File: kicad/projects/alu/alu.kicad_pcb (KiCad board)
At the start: 2 copper layers, 203.2 x 97.8 mm, 56 parts, among them J1 ACC_CONTENTS, J2 RES_AEQB_CRYBRW_OUT, J3 Control_signal_backplane, J4 Bus_connection, J5 Aux_connection, J6 TOP_POWER, J7 LED_CONTROL, U1 74HC04, U10 74HC157, U11 74HC157, U12 74HC245, U13 74HC245, U2 74LS181, U3 74LS181, U4 74HCT245, U5 74LS181, U6 74HCT245, U7 74LS181, U8 74HC157, U9 74HC157

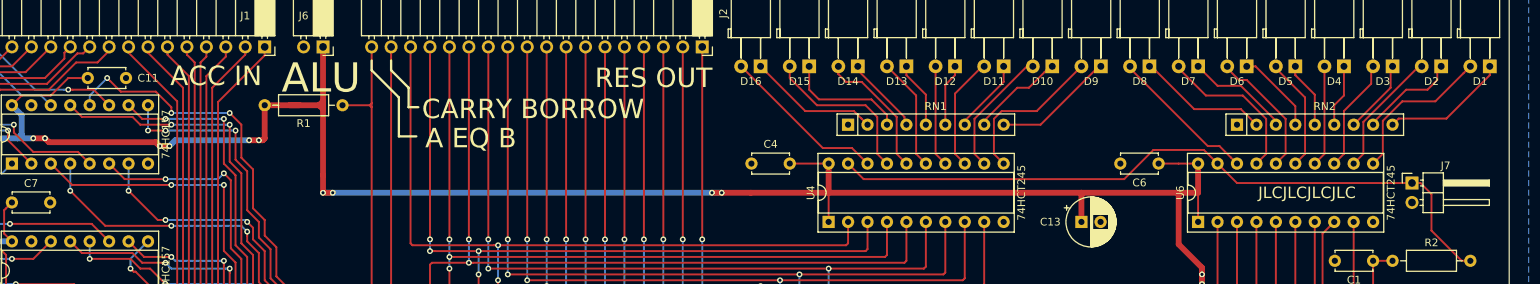
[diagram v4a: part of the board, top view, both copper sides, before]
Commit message: Better labels on ALU. Top power and LED control on register.
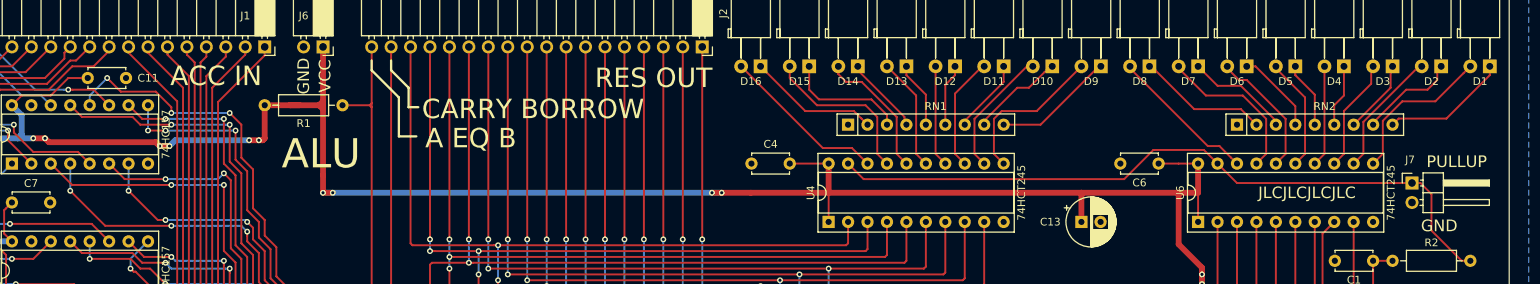
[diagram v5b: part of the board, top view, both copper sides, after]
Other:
- board text added: "GND"
- board text added: "PULLUP"
- board text added: "VCC"
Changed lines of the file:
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@@
   (general
     (thickness 1.6)
-    (drawings 22)
+    (drawings 26)
     (tracks 2059)
     (zones 0)
@@
     (descr "Through hole angled pin header, 1x02, 2.54mm pitch, 6mm pin length, single row")
     (tags "Through hole angled pin header THT 1x02 2.54mm single row")
-    (fp_text reference J7 (at 4.385 -2.27) (layer F.SilkS)
+    (fp_text reference J7 (at -0.254 -3.048) (layer F.SilkS)
       (effects (font (size 1 1) (thickness 0.15)))
     )
@@
     )
   )
+  (gr_text GND (at 247.396 81.788) (layer F.SilkS)
+    (effects (font (size 1.524 1.524) (thickness 0.254)))
+  )
+  (gr_text PULLUP (at 249.682 73.406) (layer F.SilkS)
+    (effects (font (size 1.524 1.524) (thickness 0.254)))
+  )
+  (gr_text GND (at 99.06 62.23 90) (layer F.SilkS)
+    (effects (font (size 1.524 1.524) (thickness 0.254)))
+  )
+  (gr_text VCC (at 101.854 62.23 90) (layer F.SilkS)
+    (effects (font (size 1.524 1.524) (thickness 0.254)))
+  )
   (gr_arc (start 55.245 144.145) (end 53.34 144.145) (angle -90) (layer Edge.Cuts) (width 0.05))
   (gr_arc (start 55.245 50.165) (end 55.245 48.26) (angle -90) (layer Edge.Cuts) (width 0.05))
@@
     (effects (font (size 1.5 1.5) (thickness 0.3)))
   )
-  (gr_text ALU (at 101.346 62.484) (layer F.SilkS)
+  (gr_text ALU (at 101.346 72.39) (layer F.SilkS)
     (effects (font (size 3.81 3.81) (thickness 0.381)))
   )
@@
   (segment (start 69.088 89.408) (end 61.468 89.408) (width 0.254) (layer F.Cu) (net 87))
   (via (at 59.182 89.408012) (size 0.762) (drill 0.4) (layers F.Cu B.Cu) (net 87))
+  (segment (start 59.182012 89.408) (end 59.182 89.408012) (width 0.254) (layer B.Cu) (net 87))
+  (segment (start 61.468 89.408) (end 59.182012 89.408) (width 0.254) (layer B.Cu) (net 87))
+  (segment (start 59.182 88.842327) (end 59.182 89.408012) (width 0.254) (layer F.Cu) (net 87))
+  (segment (start 58.42 64.008) (end 58.42 84.711981) (width 0.254) (layer F.Cu) (net 87))
+  (segment (start 59.182 85.473981) (end 59.182 88.842327) (width 0.254) (layer F.Cu) (net 87))
+  (segment (start 71.12 58.42) (end 69.342 60.198) (width 0.254) (layer F.Cu) (net 87))
+  (segment (start 69.342 60.198) (end 68.58 60.198) (width 0.254) (layer F.Cu) (net 87))
+  (segment (start 68.58 60.198) (end 65.532 63.246) (width 0.254) (layer F.Cu) (net 87))
   (segment (start 65.532 63.246) (end 59.182 63.246) (width 0.254) (layer F.Cu) (net 87))
   (segment (start 58.42 84.711981) (end 59.182 85.473981) (width 0.254) (layer F.Cu) (net 87))
-  (segment (start 59.182 85.473981) (end 59.182 88.842327) (width 0.254) (layer F.Cu) (net 87))
-  (segment (start 58.42 64.008) (end 58.42 84.711981) (width 0.254) (layer F.Cu) (net 87))
   (segment (start 59.182 63.246) (end 58.42 64.008) (width 0.254) (layer F.Cu) (net 87))
-  (segment (start 69.508001 59.269999) (end 65.532 63.246) (width 0.254) (layer F.Cu) (net 87))
-  (segment (start 59.182 88.842327) (end 59.182 89.408012) (width 0.254) (layer F.Cu) (net 87))
-  (segment (start 70.270001 59.269999) (end 69.508001 59.269999) (width 0.254) (layer F.Cu) (net 87))
-  (segment (start 71.12 58.42) (end 70.270001 59.269999) (width 0.254) (layer F.Cu) (net 87))
-  (segment (start 59.182012 89.408) (end 59.182 89.408012) (width 0.254) (layer B.Cu) (net 87))
-  (segment (start 61.468 89.408) (end 59.182012 89.408) (width 0.254) (layer B.Cu) (net 87))
   (segment (start 62.23 90.17) (end 63.5 91.44) (width 0.254) (layer F.Cu) (net 88))
-  (segment (start 69.342 60.452) (end 65.786 64.008) (width 0.254) (layer F.Cu) (net 88))
-  (segment (start 73.66 58.928) (end 72.136 60.452) (width 0.254) (layer F.Cu) (net 88))
-  (segment (start 72.136 60.452) (end 69.342 60.452) (width 0.254) (layer F.Cu) (net 88))
+  (segment (start 68.834 60.96) (end 65.786 64.008) (width 0.254) (layer F.Cu) (net 88))
   (segment (start 59.182 84.582) (end 60.198 85.598) (width 0.254) (layer F.Cu) (net 88))
+  (segment (start 71.628 60.96) (end 68.834 60.96) (width 0.254) (layer F.Cu) (net 88))
+  (segment (start 60.198 89.662) (end 60.706 90.17) (width 0.254) (layer F.Cu) (net 88))
   (segment (start 73.66 58.42) (end 73.66 58.928) (width 0.254) (layer F.Cu) (net 88))
-  (segment (start 65.786 64.008) (end 59.436 64.008) (width 0.254) (layer F.Cu) (net 88))
+  (segment (start 73.66 58.928) (end 71.628 60.96) (width 0.254) (layer F.Cu) (net 88))
   (segment (start 59.182 64.262) (end 59.182 84.582) (width 0.254) (layer F.Cu) (net 88))
+  (segment (start 65.786 64.008) (end 59.436 64.008) (width 0.254) (layer F.Cu) (net 88))
   (segment (start 59.436 64.008) (end 59.182 64.262) (width 0.254) (layer F.Cu) (net 88))
-  (segment (start 60.706 90.17) (end 62.23 90.17) (width 0.254) (layer F.Cu) (net 88))
   (segment (start 60.198 85.598) (end 60.198 89.662) (width 0.254) (layer F.Cu) (net 88))
-  (segment (start 60.198 89.662) (end 60.706 90.17) (width 0.254) (layer F.Cu) (net 88))
+  (segment (start 60.706 90.17) (end 62.23 90.17) (width 0.254) (layer F.Cu) (net 88))
   (segment (start 68.834 98.806) (end 66.04 101.6) (width 0.254) (layer F.Cu) (net 89))
   (segment (start 75.438 98.806) (end 68.834 98.806) (width 0.254) (layer F.Cu) (net 89))

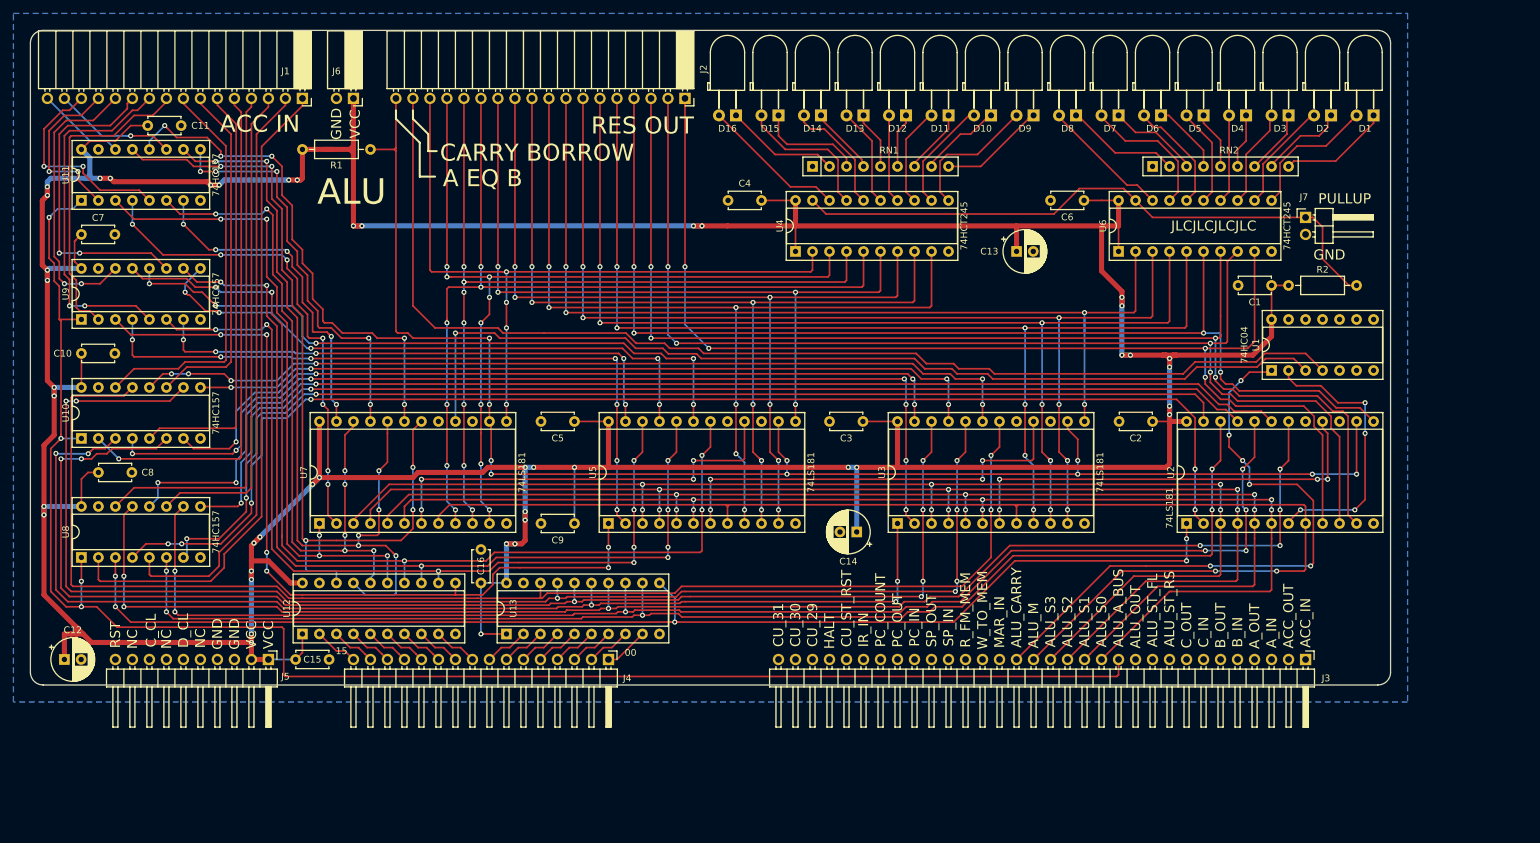
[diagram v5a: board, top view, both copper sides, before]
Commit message: Add HCT output buffer from 74LS181 on ALU.
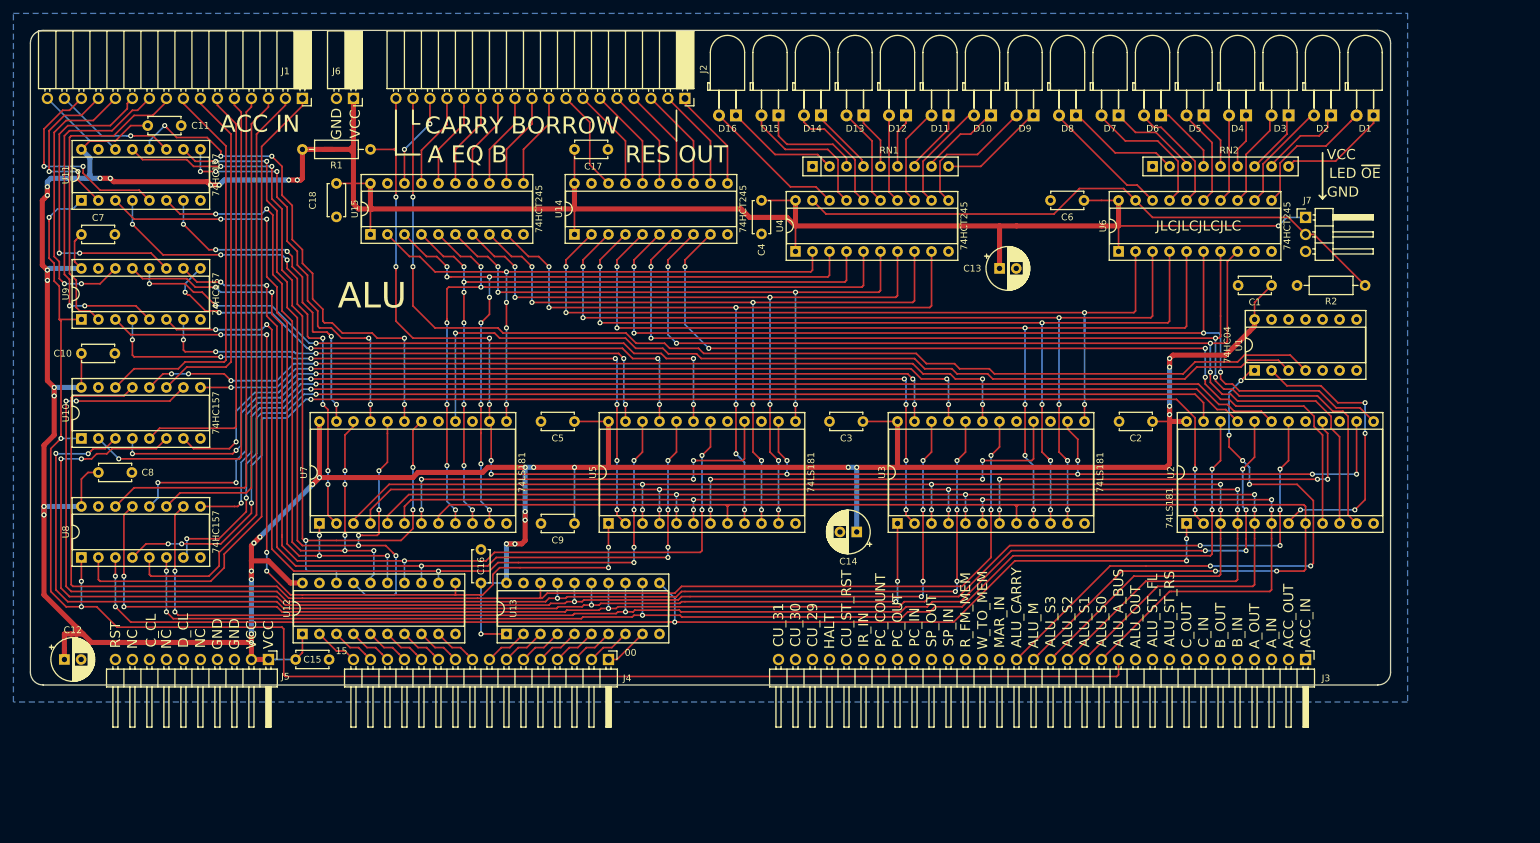
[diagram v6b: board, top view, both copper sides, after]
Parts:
- added C17: 0.1uF, Capacitor_THT:C_Disc_D4.7mm_W2.5mm_P5.00mm, F.Cu at (134.6, 66.0)
- added C18: 0.1uF, Capacitor_THT:C_Disc_D4.7mm_W2.5mm_P5.00mm, F.Cu at (99.1, 71.1)
- added U14: 74HCT245, Package_DIP:DIP-20_W7.62mm_Socket, F.Cu at (134.6, 78.7)
- added U15: 74HCT245, Package_DIP:DIP-20_W7.62mm_Socket, F.Cu at (104.1, 78.7)
- J7: footprint Connector_PinHeader_2.54mm:PinHeader_1x02_P2.54mm_Horizontal -> Connector_PinHeader_2.54mm:PinHeader_1x03_P2.54mm_Horizontal
- moved R2 11.4 mm to (252.7, 86.4), turned to 180 degrees
- moved C13 3.59 mm to (198.1, 83.8)
- moved U1 2.54 mm to (236.2, 99.1)
- turned C4 to 270 degrees
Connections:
- J2 pad 1: /RES_00 -> /RES_HC_BUF_00
- J2 pad 10: /RES_09 -> /RES_HC_BUF_09
- J2 pad 11: /RES_10 -> /RES_HC_BUF_10
- J2 pad 12: /RES_11 -> /RES_HC_BUF_11
- J2 pad 13: /RES_12 -> /RES_HC_BUF_12
- J2 pad 14: /RES_13 -> /RES_HC_BUF_13
- J2 pad 15: /RES_14 -> /RES_HC_BUF_14
- J2 pad 16: /RES_15 -> /RES_HC_BUF_15
- J2 pad 2: /RES_01 -> /RES_HC_BUF_01
- J2 pad 3: /RES_02 -> /RES_HC_BUF_02
- J2 pad 4: /RES_03 -> /RES_HC_BUF_03
- J2 pad 5: /RES_04 -> /RES_HC_BUF_04
- J2 pad 6: /RES_05 -> /RES_HC_BUF_05
- J2 pad 7: /RES_06 -> /RES_HC_BUF_06
- J2 pad 8: /RES_07 -> /RES_HC_BUF_07
- J2 pad 9: /RES_08 -> /RES_HC_BUF_08
- J7 pad 1: /LED_CONTROL -> VCC
- J7 pad 2: GND -> /LED_CONTROL
- R2 pad 1: VCC -> /LED_CONTROL
- R2 pad 2: /LED_CONTROL -> GND
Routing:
- net /RES_00: track 175.1 -> 135.3 mm
- net /RES_02: track 178.6 -> 159.9 mm
- net /RES_05: track 161.2 -> 142.4 mm
- net /RES_03: track 167.1 -> 148.3 mm
- net /RES_01: track 176.1 -> 157.4 mm
- net /RES_04: track 160.4 -> 141.7 mm
- net /RES_06: track 161.2 -> 142.4 mm
- net /RES_07: track 144.6 -> 126.1 mm
- net /RES_15: track 108.2 -> 91.1 mm
- net /RES_14: track 125.4 -> 108.6 mm
- net /RES_11: track 111.4 -> 94.6 mm
- net /RES_10: track 127.9 -> 111.1 mm
- net /RES_12: track 131.3 -> 114.5 mm
- net /RES_08: track 129.4 -> 112.6 mm
- net /RES_09: track 128.9 -> 112.1 mm
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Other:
- board text added: "LED ~OE"
- board text removed: "PULLUP"

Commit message: Tech checks on ALU.
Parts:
- moved R2 46.6 mm to (209.6, 68.8)
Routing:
- net /RES_00: track 135.3 -> 154.3 mm
- net /LED_CONTROL: track 91.0 -> 83.2 mm
- net /BUS_BUF_00: track 184.5 -> 187.2 mm
- net /BUS_BUF_01: track 194.1 -> 196.0 mm
- net Net-(D15-Pad1): track 15.8 -> 14.1 mm
- net /BUS_BUF_02: track 205.3 -> 206.5 mm
- net /BUS_BUF_03: track 215.6 -> 216.8 mm

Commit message: Alu tech checks.
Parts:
- RN1, RN2: value R_Network08_US -> 2K
- turned C13 to 270 degrees
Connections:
- net /RES_HC_BUF_00 renamed /RES_HCT_BUF_00
- net /RES_HC_BUF_01 renamed /RES_HCT_BUF_01
- net /RES_HC_BUF_02 renamed /RES_HCT_BUF_02
- net /RES_HC_BUF_03 renamed /RES_HCT_BUF_03
- net /RES_HC_BUF_04 renamed /RES_HCT_BUF_04
- net /RES_HC_BUF_05 renamed /RES_HCT_BUF_05
- net /RES_HC_BUF_06 renamed /RES_HCT_BUF_06
- net /RES_HC_BUF_07 renamed /RES_HCT_BUF_07
- net /RES_HC_BUF_08 renamed /RES_HCT_BUF_08
- net /RES_HC_BUF_09 renamed /RES_HCT_BUF_09
- net /RES_HC_BUF_10 renamed /RES_HCT_BUF_10
- net /RES_HC_BUF_11 renamed /RES_HCT_BUF_11
- net /RES_HC_BUF_12 renamed /RES_HCT_BUF_12
- net /RES_HC_BUF_13 renamed /RES_HCT_BUF_13
- net /RES_HC_BUF_14 renamed /RES_HCT_BUF_14
- net /RES_HC_BUF_15 renamed /RES_HCT_BUF_15
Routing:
- net VCC: track 749.5 -> 752.0 mm, vias 37 -> 41
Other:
- board text added: "0"
- board text added: "15"
- board text added: "V.2"
